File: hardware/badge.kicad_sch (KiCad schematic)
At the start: 2 parts

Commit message: joystick collegato, tastiera aggiornata, modulo lora, layout preliminare
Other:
- sheet keyboard ports: added none; removed KB_COL5, KB_COL6
- sheet mcu ports: added none; removed KB_COL5, KB_COL6
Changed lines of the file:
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@@
-	(wire
-		(pts
-			(xy 118.11 73.66) (xy 118.11 86.36)
-		)
-		(stroke
-			(width 0)
-			(type default)
-		)
-	)
 	(wire
 		(pts
 			(xy 133.35 60.96) (xy 158.75 60.96)
-		)
-		(stroke
-			(width 0)
-			(type default)
-		)
-	)
-	(wire
-		(pts
-			(xy 115.57 73.66) (xy 115.57 86.36)
 		)
 		(stroke
@@
 			)
 		)
-		(pin "KB_COL5" output
-			(at 115.57 86.36 90)
-			(effects
-				(font
-					(size 1.27 1.27)
-				)
-				(justify right)
-			)
-		)
-		(pin "KB_COL6" output
-			(at 118.11 86.36 90)
-			(effects
-				(font
-					(size 1.27 1.27)
-				)
-				(justify right)
-			)
-		)
 		(pin "KB_COL0" output
 			(at 102.87 86.36 90)
@@
 			(effects
 				(font
-					(size 1.27 1.27)
-				)
-				(justify left)
-			)
-		)
-		(pin "KB_COL5" input
-			(at 115.57 73.66 270)
-			(effects
-				(font
-					(size 1.27 1.27)
-				)
-				(justify left)
-			)
-		)
-		(pin "KB_COL6" input
-			(at 118.11 73.66 270)
-			(effects
-				(font

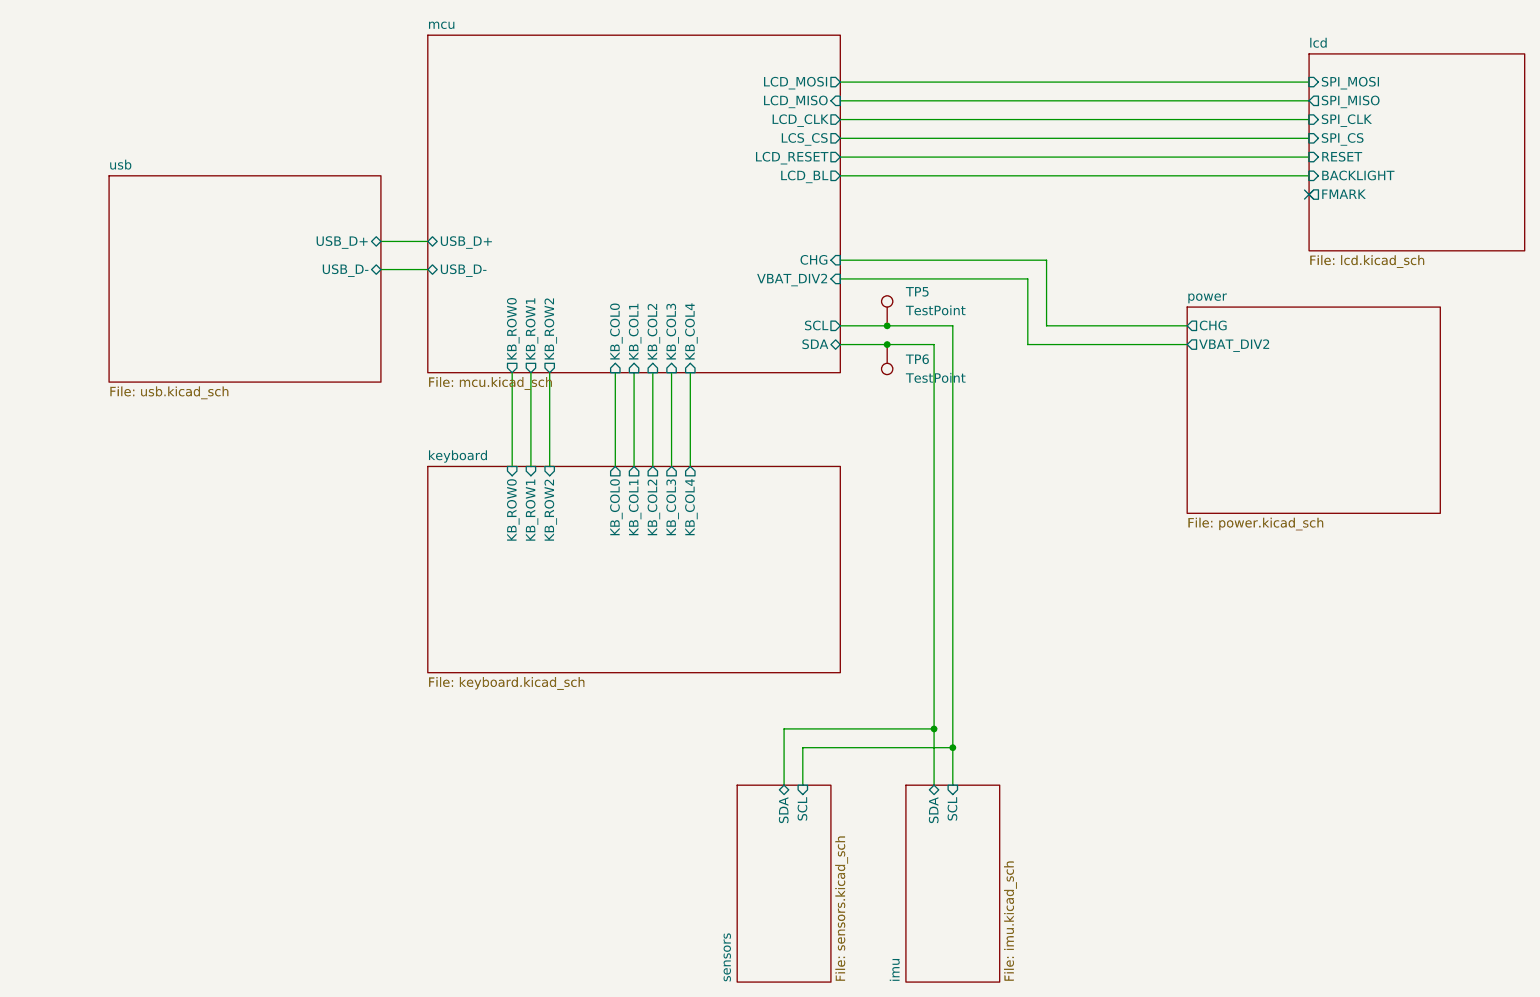
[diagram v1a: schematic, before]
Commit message: Add audio subsystem
This adds a speaker and an I2s DAC+amplifier based on MAX98357A
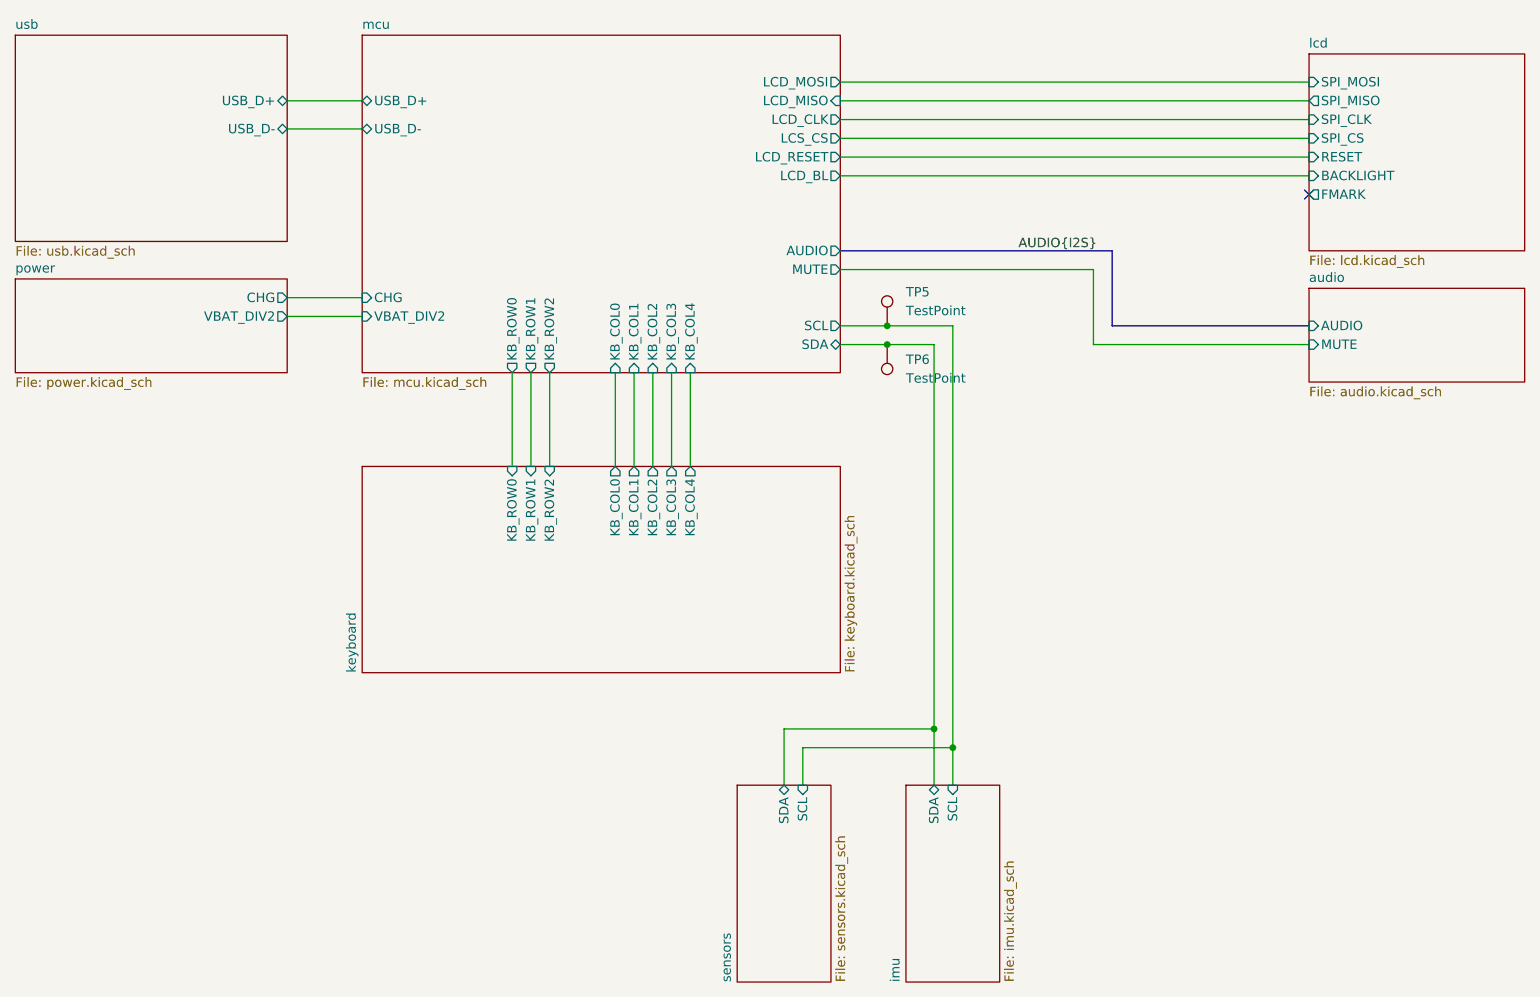
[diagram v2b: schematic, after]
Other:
- added sheet audio (audio.kicad_sch)
- sheet mcu ports: added AUDIO, MUTE; removed none
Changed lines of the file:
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@@
 	(generator_version "8.0")
 	(paper "A4")
+	(bus_alias "I2S"
+		(members "BCLK" "LRCLK" "SD")
+	)
 	(junction
 		(at 139.7 67.31)
@@
 	(wire
 		(pts
-			(xy 158.75 60.96) (xy 158.75 69.85)
-		)
-		(stroke
-			(width 0)
-			(type default)
-		)
-	)
-	(wire
-		(pts
-			(xy 133.35 60.96) (xy 158.75 60.96)
-		)
-		(stroke
-			(width 0)
-			(type default)
-		)
-	)
-	(wire
-		(pts
 			(xy 113.03 73.66) (xy 113.03 86.36)
 		)
@@
 		)
 	)
+	(bus
+		(pts
+			(xy 133.35 57.15) (xy 170.18 57.15)
+		)
+		(stroke
+			(width 0)
+			(type default)
+		)
+	)
 	(wire
 		(pts
@@
 	(wire
 		(pts
-			(xy 71.12 59.69) (xy 77.47 59.69)
-		)
-		(stroke
-			(width 0)
-			(type default)
-		)
-	)
-	(wire
-		(pts
 			(xy 133.35 69.85) (xy 139.7 69.85)
 		)
@@
 	(wire
 		(pts
+			(xy 58.42 63.5) (xy 68.58 63.5)
+		)
+		(stroke
+			(width 0)
+			(type default)
+		)
+	)
+	(wire
+		(pts
 			(xy 133.35 41.91) (xy 196.85 41.91)
 		)
@@
 	(wire
 		(pts
-			(xy 71.12 55.88) (xy 77.47 55.88)
-		)
-		(stroke
-			(width 0)
-			(type default)
-		)
-	)
-	(wire
-		(pts
 			(xy 110.49 73.66) (xy 110.49 86.36)
 		)
@@
 		)
 	)
-	(wire
-		(pts
-			(xy 158.75 69.85) (xy 180.34 69.85)
+	(bus
+		(pts
+			(xy 170.18 57.15) (xy 170.18 67.31)
+		)
+		(stroke
+			(width 0)
+			(type default)
+		)
+	)
+	(wire
+		(pts
+			(xy 196.85 69.85) (xy 167.64 69.85)
 		)
 		(stroke
@@
 	(wire
 		(pts
-			(xy 133.35 58.42) (xy 161.29 58.42)
-		)
-		(stroke
-			(width 0)
-			(type default)
-		)
-	)
-	(wire
-		(pts
 			(xy 139.7 69.85) (xy 146.05 69.85)
 		)
@@
 	(wire
 		(pts
+			(xy 58.42 66.04) (xy 68.58 66.04)
+		)
+		(stroke
+			(width 0)
+			(type default)
+		)
+	)
+	(wire
+		(pts
 			(xy 105.41 73.66) (xy 105.41 86.36)
 		)
@@
 	(wire
 		(pts
-			(xy 161.29 67.31) (xy 180.34 67.31)
+			(xy 58.42 36.83) (xy 68.58 36.83)
 		)
 		(stroke
@@
 	(wire
 		(pts
+			(xy 167.64 69.85) (xy 167.64 59.69)
+		)
+		(stroke
+			(width 0)
+			(type default)
+		)
+	)
+	(wire
+		(pts
 			(xy 128.27 124.46) (xy 148.59 124.46)
 		)
@@
 	(wire
 		(pts
+			(xy 58.42 40.64) (xy 68.58 40.64)
+		)
+		(stroke
+			(width 0)
+			(type default)
+		)
+	)
+	(bus
+		(pts
+			(xy 170.18 67.31) (xy 196.85 67.31)
+		)
+		(stroke
+			(width 0)
+			(type default)
+		)
+	)
+	(wire
+		(pts
 			(xy 139.7 67.31) (xy 148.59 67.31)
 		)
@@
 	(wire
 		(pts
-			(xy 161.29 58.42) (xy 161.29 67.31)
-		)
-		(stroke
-			(width 0)
-			(type default)
+			(xy 133.35 59.69) (xy 167.64 59.69)
+		)
+		(stroke
+			(width 0)
+			(type default)
+		)
+	)
+	(label "AUDIO{I2S}"
+		(at 157.48 57.15 0)
+		(fields_autoplaced yes)
+		(effects
+			(font
+				(size 1.27 1.27)
+			)
+			(justify left bottom)
 		)
 	)
@@
 	)
 	(sheet
-		(at 34.29 46.99)
+		(at 21.59 27.94)
 		(size 36.83 27.94)
 		(fields_autoplaced yes)
@@
 		)
 		(property "Sheetname" "usb"
-			(at 34.29 46.2784 0)
+			(at 21.59 27.2284 0)
 			(effects
 				(font
@@
 		)
 		(property "Sheetfile" "usb.kicad_sch"
-			(at 34.29 75.5146 0)
+			(at 21.59 56.4646 0)
 			(effects
 				(font
@@
 		)
 		(pin "USB_D-" bidirectional
-			(at 71.12 59.69 0)
+			(at 58.42 40.64 0)
 			(effects
 				(font
@@
 		)
 		(pin "USB_D+" bidirectional
-			(at 71.12 55.88 0)
+			(at 58.42 36.83 0)
 			(effects
 				(font
@@
 	)
 	(sheet
-		(at 77.47 86.36)
-		(size 55.88 27.94)
+		(at 196.85 62.23)
+		(size 29.21 12.7)
 		(fields_autoplaced yes)
 		(stroke
@@
 			(color 0 0 0 0.0000)
 		)
+		(property "Sheetname" "audio"
+			(at 196.85 61.5184 0)
+			(effects
+				(font
+					(size 1.27 1.27)
+				)
+				(justify left bottom)
+			)
+		)
+		(property "Sheetfile" "audio.kicad_sch"
+			(at 196.85 75.5146 0)
+			(effects
+				(font
+					(size 1.27 1.27)
+				)
+				(justify left top)
+			)
+		)
+		(pin "AUDIO" input
+			(at 196.85 67.31 180)
+			(effects
+				(font
+					(size 1.27 1.27)
+				)
+				(justify left)
+			)
+		)
+		(pin "MUTE" input
+			(at 196.85 69.85 180)
+			(effects
+				(font
+					(size 1.27 1.27)
+				)
+				(justify left)
+			)
+		)
+		(instances
+			(project "badge"
+				(path "/dc4a3d77-b0f8-4e90-a4be-3e93c7025348"
+					(page "9")
+				)
+			)
+		)
+	)
+	(sheet
+		(at 68.58 86.36)
+		(size 64.77 27.94)
+		(fields_autoplaced yes)
+		(stroke
+			(width 0.1524)
+			(type solid)
+		)
+		(fill
+			(color 0 0 0 0.0000)
+		)
 		(property "Sheetname" "keyboard"
-			(at 77.47 85.6484 0)
+			(at 67.8684 114.3 90)
 			(effects
 				(font
@@
 		)
 		(property "Sheetfile" "keyboard.kicad_sch"
-			(at 77.47 114.8846 0)
+			(at 133.9346 114.3 90)
 			(effects
 				(font
@@
 	)
 	(sheet
-		(at 77.47 27.94)
-		(size 55.88 45.72)
+		(at 68.58 27.94)
+		(size 64.77 45.72)
 		(fields_autoplaced yes)
 		(stroke
@@
 		)
 		(property "Sheetname" "mcu"
-			(at 77.47 27.2284 0)
+			(at 68.58 27.2284 0)
 			(effects
 				(font
@@
 		)
 		(property "Sheetfile" "mcu.kicad_sch"
-			(at 77.47 74.2446 0)
+			(at 68.58 74.2446 0)
 			(effects
 				(font
@@
 		)
 		(pin "CHG" input
-			(at 133.35 58.42 0)
-			(effects
-				(font
-					(size 1.27 1.27)
-				)
-				(justify right)
+			(at 68.58 63.5 180)
+			(effects
+				(font
+					(size 1.27 1.27)
+				)
+				(justify left)
 			)
 		)
@@
 		)
 		(pin "USB_D-" bidirectional
-			(at 77.47 59.69 180)
+			(at 68.58 40.64 180)
 			(effects
 				(font
@@
 		)
 		(pin "USB_D+" bidirectional
-			(at 77.47 55.88 180)
+			(at 68.58 36.83 180)
 			(effects
 				(font
@@
 		)
 		(pin "VBAT_DIV2" input
-			(at 133.35 60.96 0)
+			(at 68.58 66.04 180)
+			(effects
+				(font
+					(size 1.27 1.27)
+				)
+				(justify left)
+			)
+		)
+		(pin "AUDIO" output
+			(at 133.35 57.15 0)
+			(effects
+				(font
+					(size 1.27 1.27)
+				)
+				(justify right)
+			)
+		)
+		(pin "MUTE" output
+			(at 133.35 59.69 0)
 			(effects
 				(font
@@
 	)
 	(sheet
-		(at 180.34 64.77)
-		(size 34.29 27.94)
+		(at 21.59 60.96)
+		(size 36.83 12.7)
 		(fields_autoplaced yes)
 		(stroke
@@
 		)
 		(property "Sheetname" "power"
-			(at 180.34 64.0584 0)
+			(at 21.59 60.2484 0)
 			(effects
 				(font
@@
 		)
 		(property "Sheetfile" "power.kicad_sch"
-			(at 180.34 93.2946 0)
+			(at 21.59 74.2446 0)
 			(effects
 				(font
@@
 		)
 		(pin "CHG" output
-			(at 180.34 67.31 180)
-			(effects
-				(font
-					(size 1.27 1.27)
-				)
-				(justify left)
+			(at 58.42 63.5 0)
+			(effects
+				(font
+					(size 1.27 1.27)
+				)
+				(justify right)
 			)
 		)
 		(pin "VBAT_DIV2" output
-			(at 180.34 69.85 180)
-			(effects
-				(font
-					(size 1.27 1.27)
-				)
-				(justify left)
-			)
-		)
+			(at 58.42 66.04 0)
+			(effects
+				(font
+					(size 1.27 1.27)
+				)
+				(justify right)
+			)
+		)

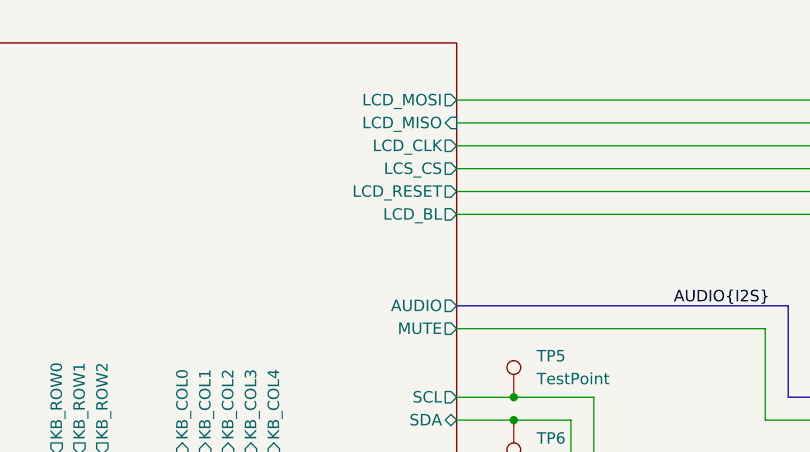
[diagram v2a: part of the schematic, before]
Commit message: add PCA9555PW io expander
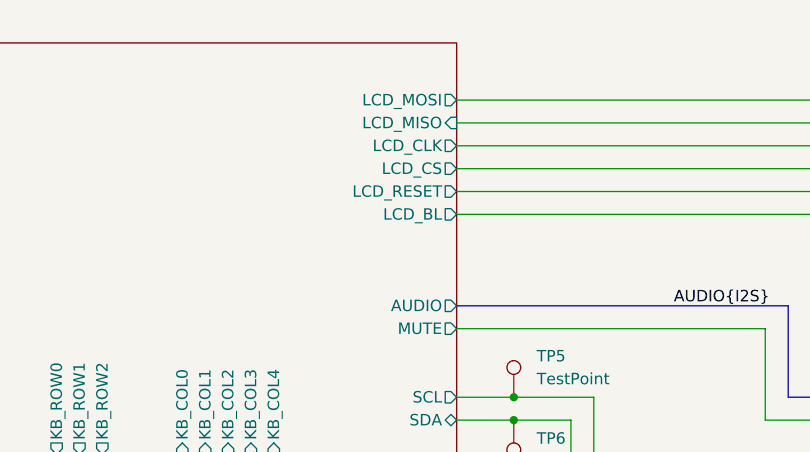
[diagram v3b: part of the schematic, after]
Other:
- sheet mcu ports: added LCD_CS; removed LCS_CS
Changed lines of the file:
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@@
-			)
-		)
-		(pin "LCS_CS" output
-			(at 133.35 41.91 0)
-			(effects
-				(font
-					(size 1.27 1.27)
-				)
-				(justify right)
 			)
 		)
@@
 			(effects
 				(font
+					(size 1.27 1.27)
+				)
+				(justify right)
+			)
+		)
+		(pin "LCD_CS" output
+			(at 133.35 41.91 0)
+			(effects
+				(font
